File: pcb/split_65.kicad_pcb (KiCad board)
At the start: 2 copper layers, 325 x 125 mm, 221 parts, among them J1 PJ-3200B-4A, J10 AVR-ISP-6, J11 Breakaway_Tabs, J12 Breakaway_Tabs, J13 Breakaway_Tabs, J14 Breakaway_Tabs, J2 AVR-ISP-6, J3 Breakaway_Tabs, J4 Breakaway_Tabs, J5 Breakaway_Tabs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

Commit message: update pcb traces
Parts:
- moved D36 15.5 mm to (212.5, 61.9)
- moved D19 15.5 mm to (131.6, 100.0)
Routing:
- net GND: track 235.6 -> 278.6 mm, vias 1 -> 3
- net GNDA: track 265.2 -> 301.0 mm, vias 1 -> 2
- net COL1-R: track 202.9 -> 175.5 mm, vias 0 -> 1
- net +5V: track 254.5 -> 278.1 mm, vias 8 -> 9
- net Net-(D19-Pad2): track 0.00 -> 7.11 mm
- net ROW3: track 155.4 -> 148.6 mm
- net Net-(D36-Pad2): track 12.1 -> 7.03 mm
- net +5VA: track 279.5 -> 283.6 mm
- net VCC: track 23.9 -> 25.2 mm
- net RESET: track 41.4 -> 40.3 mm
- net ROW0: track 193.3 -> 194.4 mm, vias 4 -> 2
- net ROW2: track 143.6 -> 144.7 mm, vias 4 -> 2
- net ROW0-R: track 206.8 -> 207.6 mm
- net MISO: track 46.6 -> 47.1 mm
- net SCL: track 159.5 -> 159.7 mm, vias 2 -> 4
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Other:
- board text added: "Split 65 PCB Rev1.0 5-17-2019"

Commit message: update silkscreen
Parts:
- moved R69 1.19 mm to (274.4, 135.7)
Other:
- board text added: "Split 65 PCB Rev1.0 10-27-2019"
- board text added: "split_65"
- board text removed: "Split 65 PCB Rev1.0 5-17-2019"

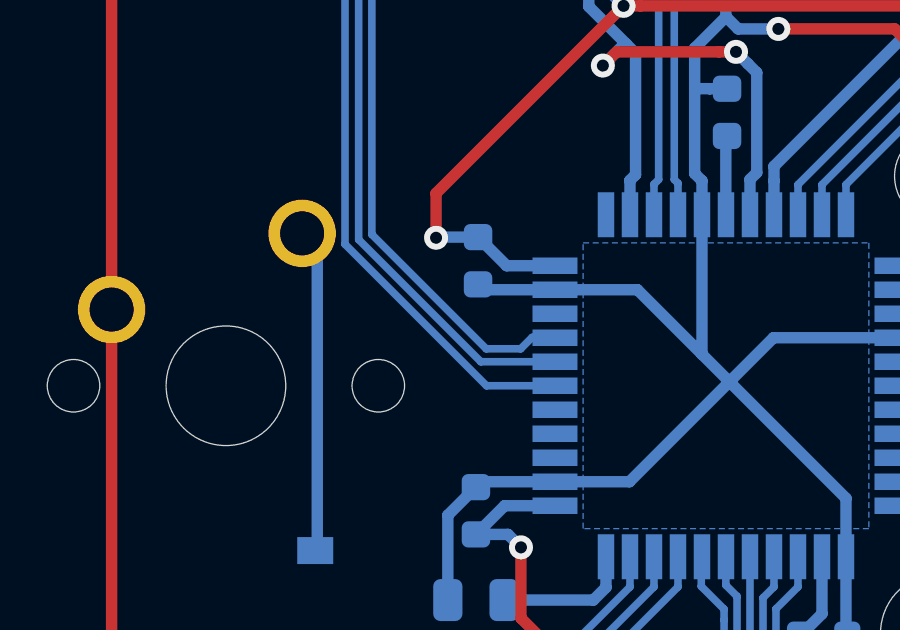
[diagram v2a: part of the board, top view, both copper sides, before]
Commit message: Added BOM, gerbers, and position
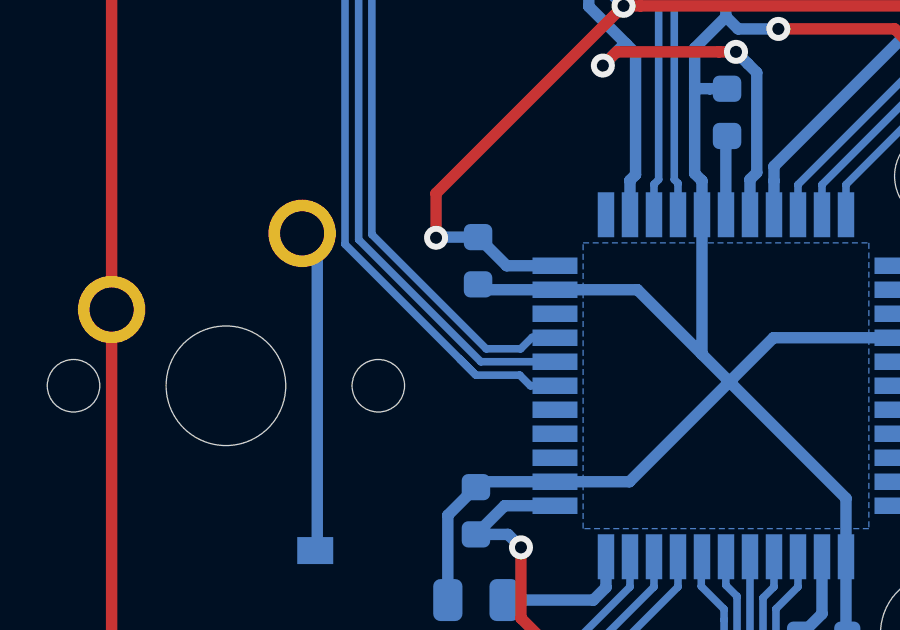
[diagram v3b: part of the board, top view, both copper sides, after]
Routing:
- net ROW0: track 194.4 -> 195.1 mm
